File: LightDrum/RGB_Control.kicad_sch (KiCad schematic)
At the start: 0 parts

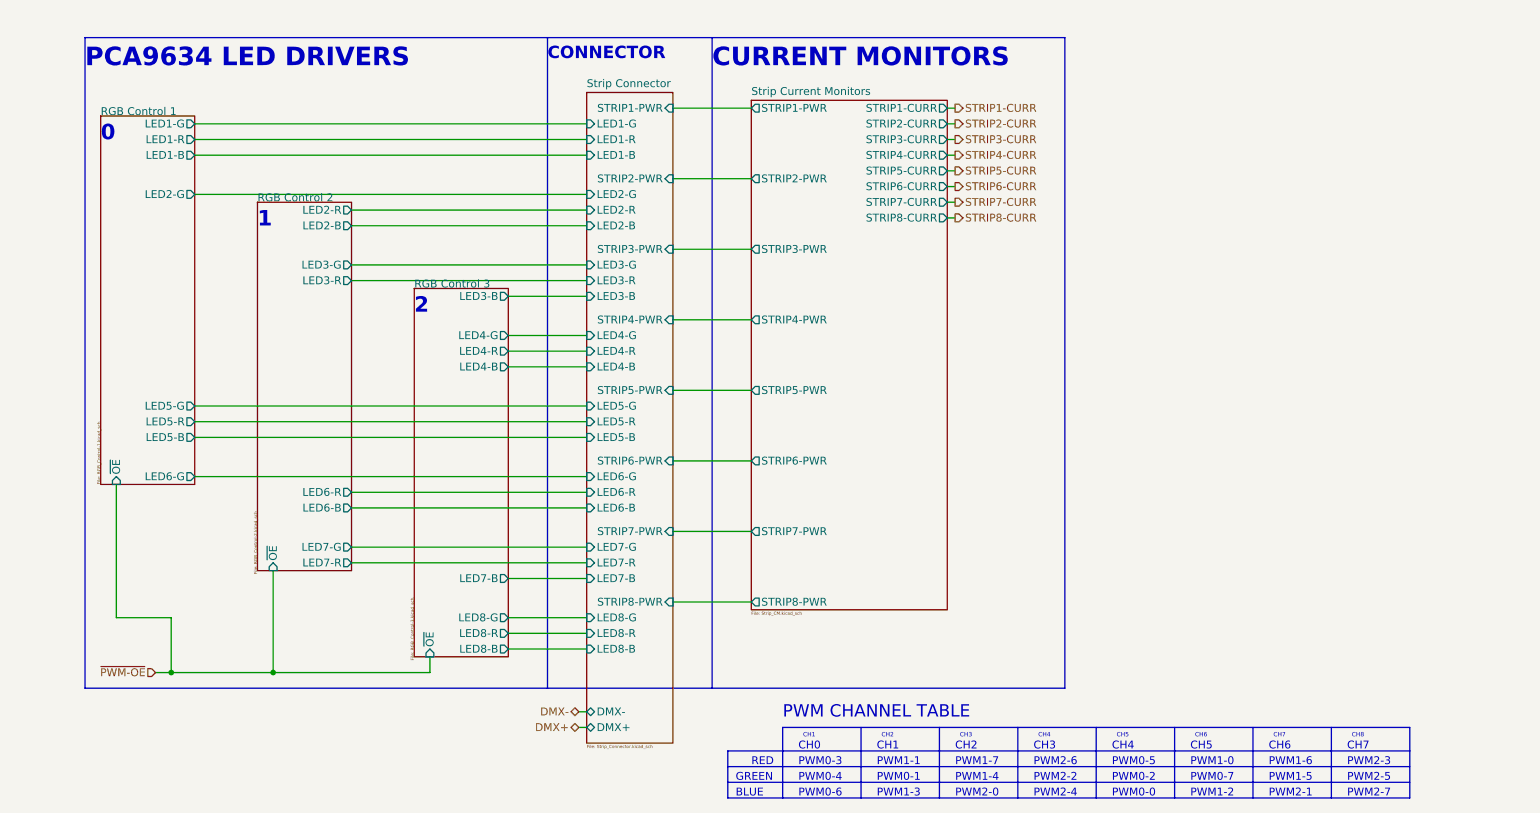
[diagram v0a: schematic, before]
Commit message: Preliminary schematic lock - Starting PCB layout
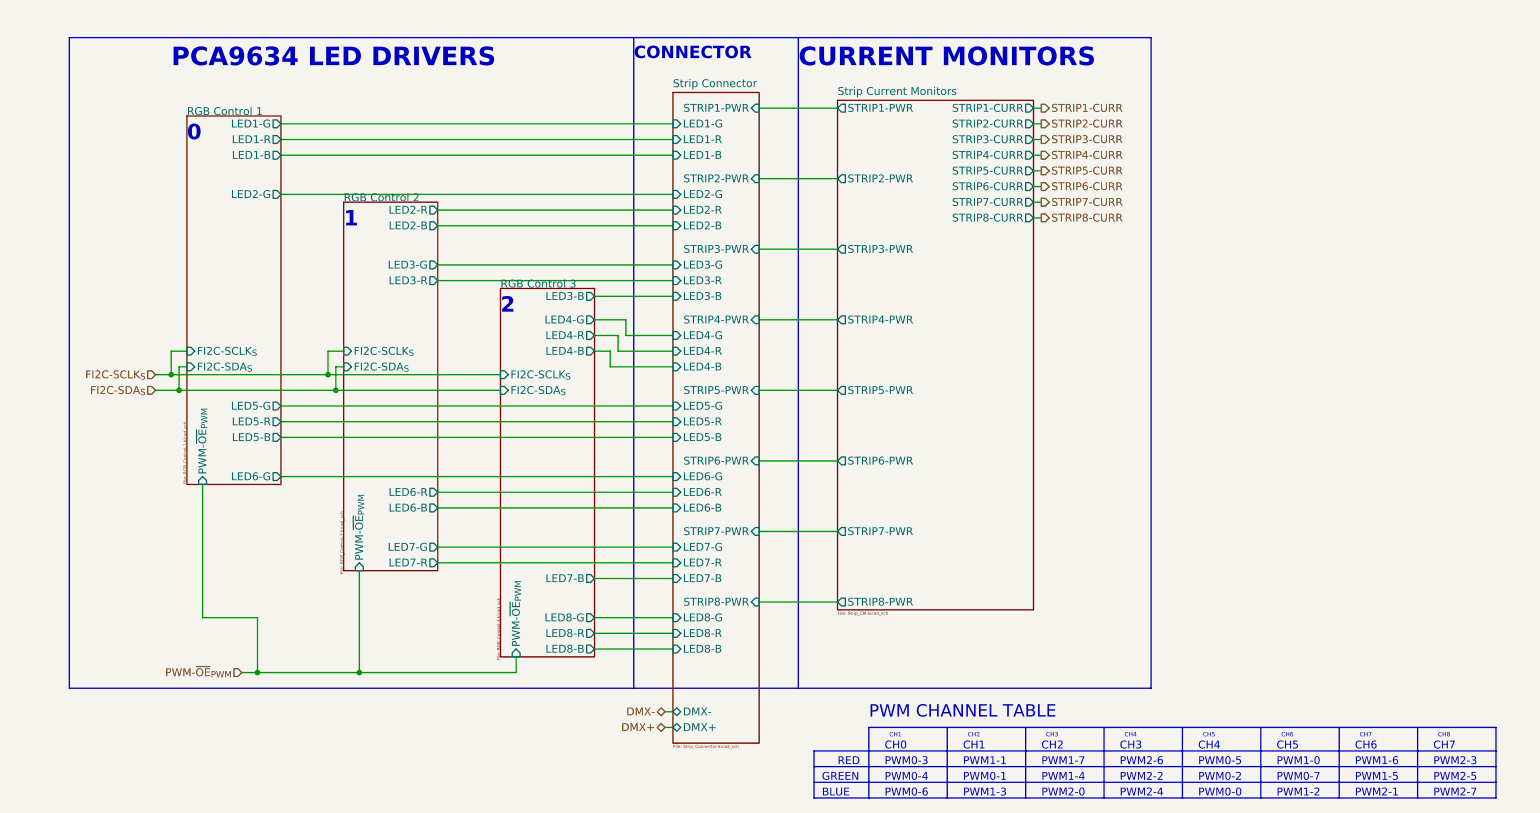
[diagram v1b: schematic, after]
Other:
- sheet RGB Control 1 ports: added FI2C-SCLK_{S}, FI2C-SDA_{S}, PWM-~{OE}_{PWM}; removed ~{OE}
- sheet RGB Control 2 ports: added FI2C-SCLK_{S}, FI2C-SDA_{S}, PWM-~{OE}_{PWM}; removed ~{OE}
- sheet RGB Control 3 ports: added FI2C-SCLK_{S}, FI2C-SDA_{S}, PWM-~{OE}_{PWM}; removed ~{OE}

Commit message: Component placement complete
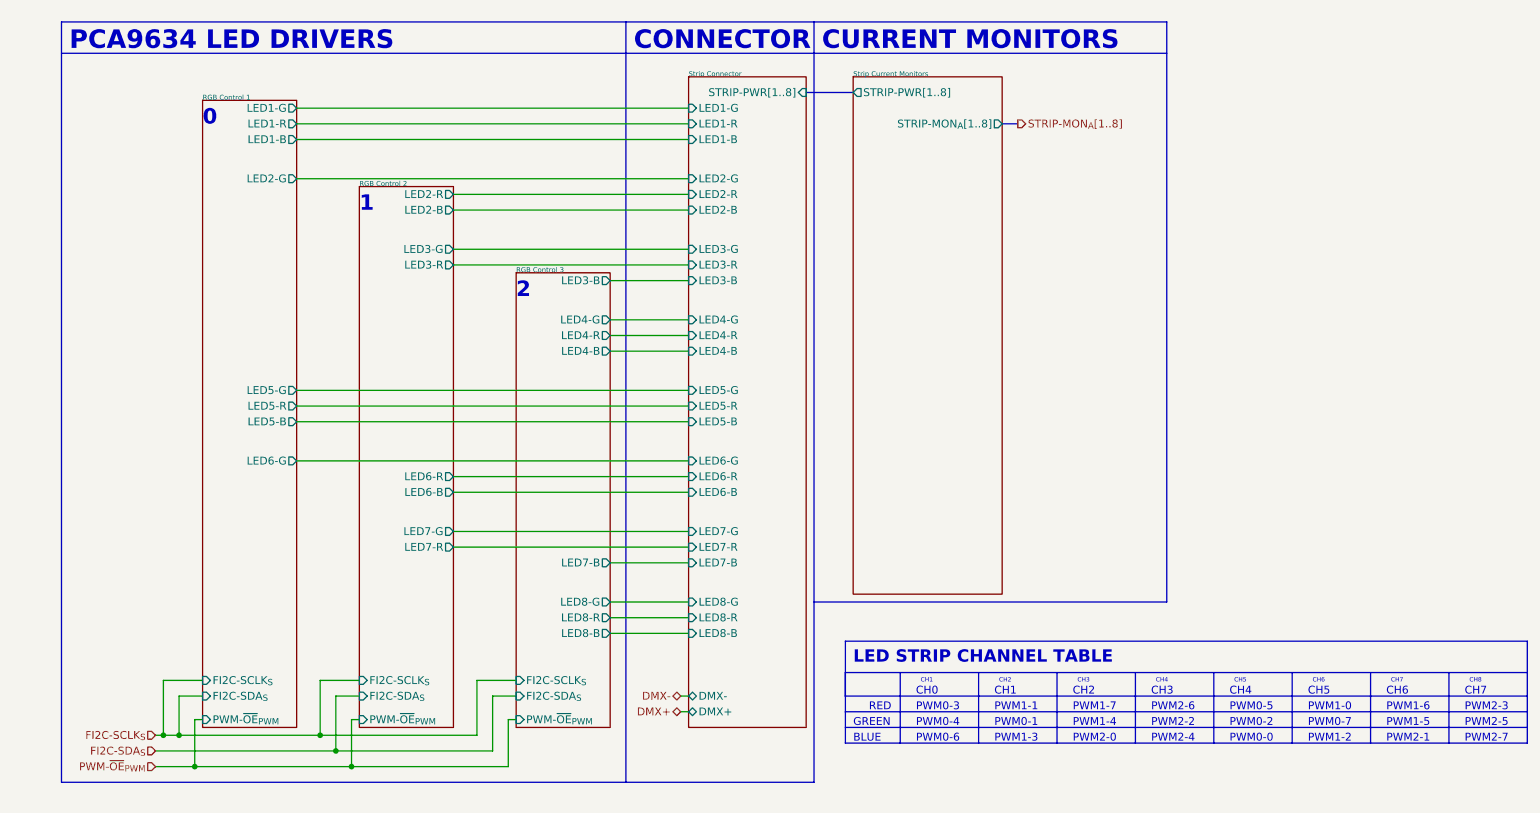
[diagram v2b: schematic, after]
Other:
- sheet Strip Connector ports: added STRIP-PWR[1..8]; removed STRIP1-PWR, STRIP2-PWR, STRIP3-PWR, STRIP4-PWR, STRIP5-PWR, STRIP6-PWR, STRIP7-PWR, STRIP8-PWR
- sheet Strip Current Monitors ports: added STRIP-MON_{A}[1..8], STRIP-PWR[1..8]; removed STRIP1-CURR, STRIP1-PWR, STRIP2-CURR, STRIP2-PWR, STRIP3-CURR, STRIP3-PWR, STRIP4-CURR, STRIP4-PWR, STRIP5-CURR, STRIP5-PWR, STRIP6-CURR, STRIP6-PWR, STRIP7-CURR, STRIP7-PWR, STRIP8-CURR, STRIP8-PWR
- note added: "LED STRIP CHANNEL TABLE"
- note removed: "PWM CHANNEL TABLE"

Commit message: First draft layout almost complete
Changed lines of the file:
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@@
   (junction (at 57.15 132.08) (diameter 0) (color 0 0 0 0)
   )
-  (junction (at 31.75 129.54) (diameter 0) (color 0 0 0 0)
-  )
   (junction (at 34.29 134.62) (diameter 0) (color 0 0 0 0)
   )
   (junction (at 54.61 129.54) (diameter 0) (color 0 0 0 0)
   )
+  (junction (at 31.75 132.08) (diameter 0) (color 0 0 0 0)
+  )
   (junction (at 29.21 129.54) (diameter 0) (color 0 0 0 0)
   )
@@
     (stroke (width 0) (type default))
   )
-  (wire (pts (xy 27.94 132.08) (xy 57.15 132.08))
+  (wire (pts (xy 27.94 132.08) (xy 31.75 132.08))
     (stroke (width 0) (type default))
   )
@@
     (stroke (width 0.1) (type solid))
   )
-  (wire (pts (xy 31.75 123.19) (xy 31.75 129.54))
-    (stroke (width 0) (type default))
-  )
   (wire (pts (xy 76.2 44.45) (xy 114.3 44.45))
     (stroke (width 0) (type default))
@@
     (stroke (width 0) (type default))
   )
-  (wire (pts (xy 31.75 129.54) (xy 54.61 129.54))
-    (stroke (width 0) (type default))
-  )
-  (wire (pts (xy 29.21 129.54) (xy 31.75 129.54))
+  (wire (pts (xy 29.21 129.54) (xy 54.61 129.54))
     (stroke (width 0) (type default))
   )
@@
     (stroke (width 0) (type default))
   )
+  (wire (pts (xy 31.75 123.19) (xy 31.75 132.08))
+    (stroke (width 0) (type default))
+  )
   (polyline (pts (xy 191.77 13.97) (xy 191.77 107.95))
     (stroke (width 0) (type default))
@@
     (stroke (width 0.1) (type solid))
   )
+  (wire (pts (xy 31.75 132.08) (xy 57.15 132.08))
+    (stroke (width 0) (type default))
+  )
   (polyline (pts (xy 250.19 119.38) (xy 250.19 123.19))

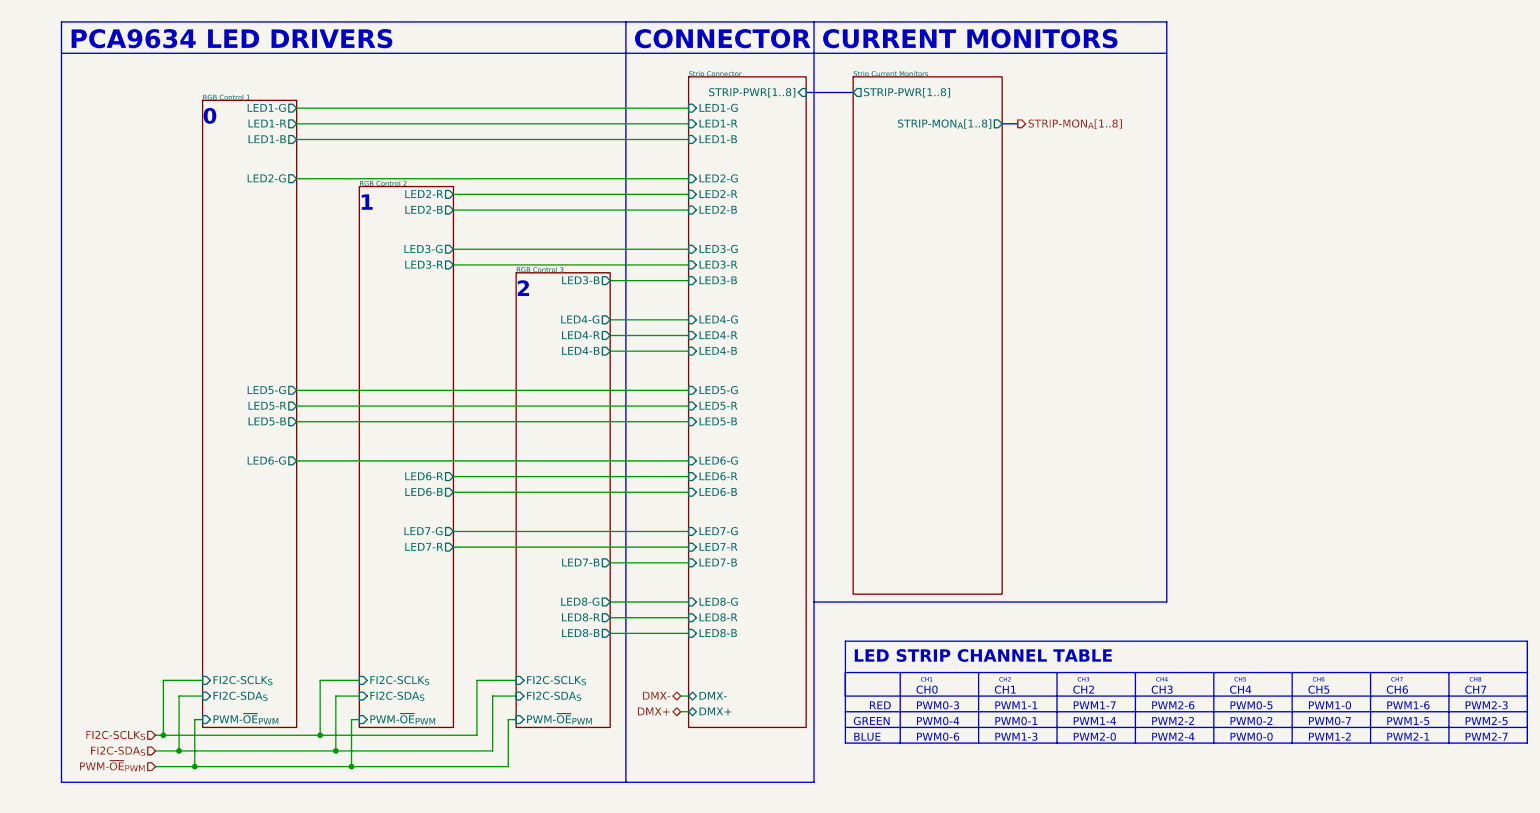
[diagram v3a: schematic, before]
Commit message: Replace DSub with much better ECU conn
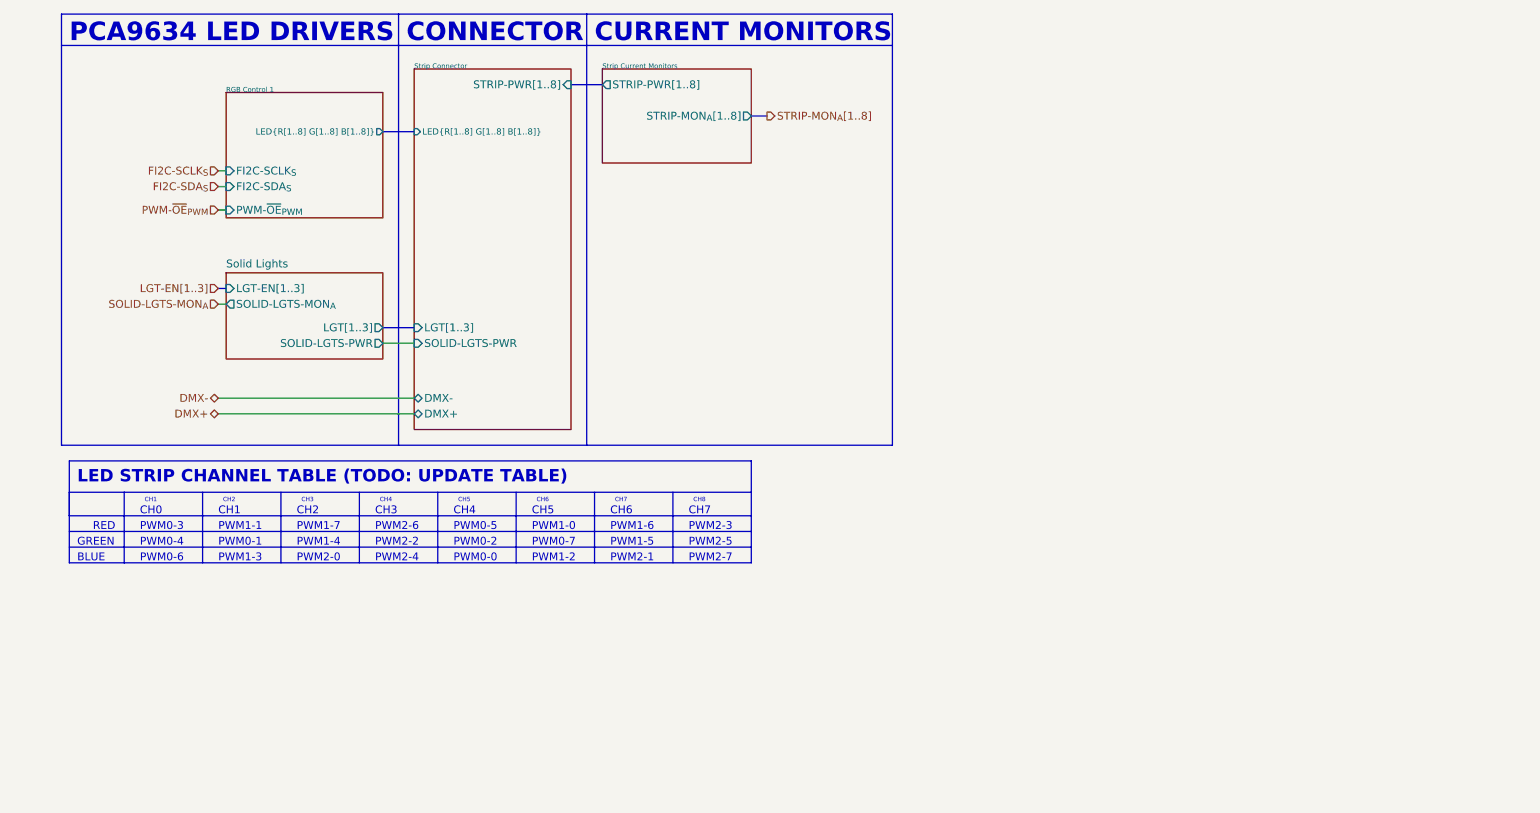
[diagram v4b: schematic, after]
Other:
- removed sheet RGB Control 2
- removed sheet RGB Control 3
- added sheet Solid Lights (SolidLights.kicad_sch)
- sheet RGB Control 1 ports: added LED{R[1..8] G[1..8] B[1..8]}; removed LED1-B, LED1-G, LED1-R, LED2-G, LED5-B, LED5-G, LED5-R, LED6-G
- sheet Strip Connector ports: added LED{R[1..8] G[1..8] B[1..8]}, LGT[1..3], SOLID-LGTS-PWR; removed LED1-B, LED1-G, LED1-R, LED2-B, LED2-G, LED2-R, LED3-B, LED3-G, LED3-R, LED4-B, LED4-G, LED4-R, LED5-B, LED5-G, LED5-R, LED6-B, LED6-G, LED6-R, LED7-B, LED7-G, LED7-R, LED8-B, LED8-G, LED8-R
- note added: "LED STRIP CHANNEL TABLE (TODO: UPDATE TABLE)"
- note removed: "0"
- note removed: "1"
- note removed: "2"
- note removed: "LED STRIP CHANNEL TABLE"

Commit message: Organize old files and generate interface gerbers
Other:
- sheet RGB Control 1 renamed RGB Control
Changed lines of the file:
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@@
     (stroke (width 0.1524) (type solid))
     (fill (color 0 0 0 0.0000))
-    (property "Sheetname" "RGB Control 1" (at 39.37 25.4 0)
+    (property "Sheetname" "RGB Control" (at 39.37 25.4 0)
       (effects (font (size 0.8 0.8)) (justify left bottom))
     )
@@
     (instances
       (project "LightDrum"
-        (path "/7f137461-fd46-4a4c-8db7-555d487fb3ca/c5b6f44f-b454-4d73-ae8d-4f0249b04054" (page "12"))
+        (path "/7f137461-fd46-4a4c-8db7-555d487fb3ca/c5b6f44f-b454-4d73-ae8d-4f0249b04054" (page "13"))
       )
     )

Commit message: (WIP) REV12 Testing and firmware dev
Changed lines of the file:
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@@
   (title_block
     (title "LightDrum")
-    (rev "REV11")
+    (rev "REV13")
     (company "Daxxn Industries")
   )
@@
   )
   (sheet (at 69.85 21.59) (size 25.4 58.42)
-    (stroke (width 0.1524) (type solid))
+    (stroke (width 0.2) (type solid))
     (fill (color 0 0 0 0.0000))
     (property "Sheetname" "Strip Connector" (at 69.85 21.59 0)
@@
   )
   (sheet (at 39.37 25.4) (size 25.4 20.32)
-    (stroke (width 0.1524) (type solid))
+    (stroke (width 0.2) (type solid))
     (fill (color 0 0 0 0.0000))
     (property "Sheetname" "RGB Control" (at 39.37 25.4 0)
@@
   )
   (sheet (at 100.33 21.59) (size 24.13 15.24)
-    (stroke (width 0.1524) (type solid))
+    (stroke (width 0.2) (type solid))
     (fill (color 0 0 0 0.0000))
     (property "Sheetname" "Strip Current Monitors" (at 100.33 21.59 0)
@@
   )
   (sheet (at 39.37 54.61) (size 25.4 13.97) (fields_autoplaced)
-    (stroke (width 0.1524) (type solid))
+    (stroke (width 0.2) (type solid))
     (fill (color 0 0 0 0.0000))
     (property "Sheetname" "Solid Lights" (at 39.37 53.8984 0)
